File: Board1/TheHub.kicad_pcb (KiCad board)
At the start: 2 copper layers, 54 parts, among them J1 ARM_ADC_1, J10 SCIENCE + WHEELS POWER CONN, J11 RFD900, J12 I2C_1 Test Point, J13 I2C_2 Test Point, J14 ARDUINO NANO LEFT, J15 GPIO Test, J16 I2C_3 Test Point, J17 12V OUT, J18 7.4V IN, J19 ANALOG SENSORS, J2 ARM_ADC_2, J20 GPS, J21 COMPASS, J22 ARDUINO NANO RIGHT, J3 ARM_PWM_OUT, J4 ARM POWER CONN, J5 NucleoF411RE, J6 SCI_ADC_1, J7 SCIENCE_PWM_OUT, J8 12V MAIN POWER, J9 WHEEL_ADC_1, U1 PRE-PCA9685, U2 PRE-ADS1115, U3 PRE-ADS1115, U4 PRE-PCA9685, U5 PRE-ADS1115, U6 LD1086DT33TR, U7 LM340MP-5.0, U9 PRE-ADS1115

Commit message: Change 3v3 regulator, change appropriate pins to sockets
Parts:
- added J23: NucleoRight, Socket_Strips:Socket_Strip_Straight_2x19_Pitch2.54mm, F.Cu at (38.1, 43.2)
- J11: footprint Pin_Headers:Pin_Header_Angled_2x08_Pitch2.54mm -> Socket_Strips:Socket_Strip_Angled_2x08_Pitch2.54mm
- J14, J22: footprint Pin_Headers:Pin_Header_Straight_1x15_Pitch2.54mm -> Socket_Strips:Socket_Strip_Straight_1x15_Pitch2.54mm
- J20: footprint Pin_Headers:Pin_Header_Straight_1x09_Pitch2.54mm -> Socket_Strips:Socket_Strip_Straight_1x09_Pitch2.54mm
- J21: footprint Pin_Headers:Pin_Header_Straight_1x06_Pitch2.54mm -> Socket_Strips:Socket_Strip_Straight_1x06_Pitch2.54mm
- J5: value NucleoF411RE -> NucleoLeft; footprint Pin_Headers:Pin_Header_Straight_2x19_Pitch2.54mm -> Socket_Strips:Socket_Strip_Straight_2x19_Pitch2.54mm
- U2, U3, U5, U9: footprint Pin_Headers:Pin_Header_Straight_1x10_Pitch2.54mm -> Socket_Strips:Socket_Strip_Straight_1x10_Pitch2.54mm
- U6: value LD1086DT33TR -> TL1963; footprint TO_SOT_Packages_SMD:TO-252-3_TabPin2 -> TO_SOT_Packages_SMD:SOT-223-3Lead_TabPin2
- moved J21 252.2 mm to (0.00, 0.00)
- moved U6 117.3 mm to (0.00, 0.00)
- moved J5 62.6 mm to (22.9, 43.2)
- moved J11 18.3 mm to (74.9, 20.3), turned to 0 degrees
- moved J22 14.2 mm to (237.5, 34.3)
- moved J14 14.2 mm to (221.0, 34.3)
- moved J20 11.7 mm to (246.4, 49.5)
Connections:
- net /AGND renamed /PA4
- net /AVDD renamed /BOOT0
- net /PA10 renamed /VBAT
- net /PA2 renamed /PC2
- net /PA3 renamed /PC3
- net /PA5 renamed Net-(J5-Pad11)
- net /PB1 renamed Net-(J5-Pad24)
- net /PB13 renamed /PA1
- net /PB14 renamed /PA0
- net /PB15 renamed Net-(J5-Pad26)
- net /PB4 renamed /PC15
- net /PB5 renamed /PH0
- net /PB8 renamed /PC12
- net /PB9 renamed /VDD
- net /PC6 renamed /PD2
- net /PC8 renamed /PC11
- net Net-(J5-Pad36) renamed /PC1
- net Net-(J5-Pad38) renamed /PC0
- J5 pad 1: /PC9 -> /PC10
- J5 pad 12: /PA12 -> /IOREF
- J5 pad 13: /PA6 -> /PA13
- J5 pad 14: /PA11 -> /RESET
- J5 pad 15: /PA7 -> /PA14
- J5 pad 16: /PB12 -> +3V3
- J5 pad 17: /PB6 -> /PA15
- J5 pad 18: Net-(J5-Pad18) -> +5V
- J5 pad 21: /PA9 -> /PB7
- J5 pad 23: /PA8 -> /PC13
- J5 pad 25: /A5 -> /PC14
- J5 pad 31: /A4 -> /PH1
- J5 pad 34: /PC4 -> /PB0
- J5 pad 6: /PC5 -> /E5V
- J5 pad 9: GND -> Net-(J5-Pad9)
- U6 pad 1: GND -> +12V
- U6 pad 2: +3V3 -> GND
- U6 pad 3: +12V -> +3V3

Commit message: Create Layout placement forRFD900 and Nucleo
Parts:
- moved J23 355.4 mm to (389.9, 94.0)
- moved J11 318.9 mm to (393.7, 28.4)
- moved J5 310.3 mm to (328.9, 94.0)
- moved J21 248.0 mm to (246.4, 27.9)
- moved D7 7.18 mm to (214.6, 34.3)
- moved R13 5.08 mm to (214.6, 36.8)
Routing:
- net Net-(D7-Pad1): track 0.00 -> 3.39 mm
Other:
- board outline added: 195.6 x 195.6 mm
- board text added: "HEATSINK UP!"
- board text added: "RFD900"
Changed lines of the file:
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@@
   (general
     (links 255)
-    (no_connects 255)
+    (no_connects 254)
     (area 0 0 0 0)
     (thickness 1.6)
-    (drawings 0)
-    (tracks 0)
+    (drawings 21)
+    (tracks 3)
     (zones 0)
     (modules 55)
@@
   )
   (module LEDs:LED_0805 (layer F.Cu)
-    (at 209.55 39.37)
+    (at 214.63 34.29)
     (descr "LED 0805 smd package")
     (tags "LED led 0805 SMD smd SMT smt smdled SMDLED smtled SMTLED")
@@
   )
   (module Resistors_SMD:R_0805 (layer F.Cu)
-    (at 209.55 36.83)
+    (at 214.63 36.83)
     (descr "Resistor SMD 0805, reflow soldering, Vishay (see dcrcw.pdf)")
     (tags "resistor 0805")
@@
   )
   (module Socket_Strips:Socket_Strip_Straight_2x19_Pitch2.54mm (layer F.Cu)
-    (at 22.86 43.18)
+    (at 328.93 93.98)
     (descr "Through hole straight socket strip, 2x19, 2.54mm pitch, double rows")
     (tags "Through hole socket strip THT 2x19 2.54mm double row")
@@
   )
   (module Socket_Strips:Socket_Strip_Angled_2x08_Pitch2.54mm (layer F.Cu)
-    (at 74.93 20.32)
+    (at 393.7 28.448)
     (descr "Through hole angled socket strip, 2x08, 2.54mm pitch, 8.51mm socket length, double rows")
     (tags "Through hole angled socket strip THT 2x08 2.54mm double row")
@@
   )
   (module Socket_Strips:Socket_Strip_Straight_1x06_Pitch2.54mm (layer F.Cu)
-    (at 0 0)
+    (at 246.38 27.94)
     (descr "Through hole straight socket strip, 1x06, 2.54mm pitch, single row")
     (tags "Through hole socket strip THT 1x06 2.54mm single row")
@@
   )
   (module Socket_Strips:Socket_Strip_Straight_2x19_Pitch2.54mm (layer F.Cu)
-    (at 38.1 43.18)
+    (at 389.89 93.98)
     (descr "Through hole straight socket strip, 2x19, 2.54mm pitch, double rows")
     (tags "Through hole socket strip THT 2x19 2.54mm double row")
@@
     )
   )
+  (gr_line (start 323.85 59.69) (end 392.43 59.69) (angle 90) (layer F.SilkS) (width 0.2))
+  (gr_line (start 392.43 142.24) (end 323.85 142.24) (angle 90) (layer F.SilkS) (width 0.2))
+  (gr_line (start 392.43 142.24) (end 392.43 59.69) (angle 90) (layer F.SilkS) (width 0.2))
+  (gr_line (start 323.85 142.24) (end 323.85 59.69) (angle 90) (layer F.SilkS) (width 0.2))
+  (gr_text "HEATSINK UP!" (at 358.14 40.64) (layer F.SilkS)
+    (effects (font (size 1.5 1.5) (thickness 0.3)))
+  )
+  (gr_text RFD900 (at 358.14 35.56) (layer F.SilkS)
+    (effects (font (size 2.54 2.54) (thickness 0.508)))
+  )
+  (gr_line (start 322.58 44.45) (end 335.28 44.45) (angle 90) (layer F.SilkS) (width 0.2))
+  (gr_line (start 322.58 52.07) (end 322.58 44.45) (angle 90) (layer F.SilkS) (width 0.2))
+  (gr_line (start 335.28 52.07) (end 322.58 52.07) (angle 90) (layer F.SilkS) (width 0.2))
+  (gr_line (start 322.58 30.48) (end 335.28 30.48) (angle 90) (layer F.SilkS) (width 0.2))
+  (gr_line (start 322.58 22.86) (end 322.58 30.48) (angle 90) (layer F.SilkS) (width 0.2))
+  (gr_line (start 335.28 22.86) (end 322.58 22.86) (angle 90) (layer F.SilkS) (width 0.2))
+  (gr_line (start 335.28 21.59) (end 335.28 22.86) (angle 90) (layer F.SilkS) (width 0.2))
+  (gr_line (start 335.28 53.34) (end 381 53.34) (angle 90) (layer F.SilkS) (width 0.2))
+  (gr_line (start 335.28 21.59) (end 335.28 53.34) (angle 90) (layer F.SilkS) (width 0.2))
+  (gr_line (start 381 21.59) (end 335.28 21.59) (angle 90) (layer F.SilkS) (width 0.2))
+  (gr_line (start 381 53.34) (end 381 21.59) (angle 90) (layer F.SilkS) (width 0.2))
+  (gr_line (start 308.61 214.63) (end 308.61 19.05) (angle 90) (layer Edge.Cuts) (width 0.15))
+  (gr_line (start 504.19 214.63) (end 308.61 214.63) (angle 90) (layer Edge.Cuts) (width 0.15))
+  (gr_line (start 504.19 19.05) (end 504.19 214.63) (angle 90) (layer Edge.Cuts) (width 0.15))
+  (gr_line (start 308.61 19.05) (end 504.19 19.05) (angle 90) (layer Edge.Cuts) (width 0.15))
+  (segment (start 215.58 36.83) (end 215.58 36.51) (width 0.25) (layer F.Cu) (net 12))
+  (segment (start 215.58 36.51) (end 213.53 34.46) (width 0.25) (layer F.Cu) (net 12))
+  (segment (start 213.53 34.46) (end 213.53 34.29) (width 0.25) (layer F.Cu) (net 12))
 )

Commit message: Determine Main Board Layout
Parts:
- moved U6 422.2 mm to (416.6, 68.6)
- moved J8 408.5 mm to (497.8, 175.3), turned to 180 degrees
- moved R11 401.8 mm to (472.4, 110.5)
- moved R12 401.8 mm to (472.4, 106.7)
- moved J17 394.9 mm to (497.8, 182.9), turned to 180 degrees
- moved R10 387.4 mm to (450.9, 106.7)
- moved J18 384.6 mm to (497.8, 194.3), turned to 180 degrees
- moved R3 371.0 mm to (426.7, 110.5)
- moved R4 369.8 mm to (426.7, 106.7)
- moved R6 363.7 mm to (462.3, 82.5)
- moved R8 357.1 mm to (462.3, 90.2)
- moved R7 356.5 mm to (462.3, 86.4)
- moved J16 353.9 mm to (478.8, 110.5), turned to 180 degrees
- moved R5 351.8 mm to (450.9, 110.5)
- moved J13 322.6 mm to (457.2, 110.5), turned to 180 degrees
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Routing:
- net Net-(J3-Pad8): track 0.00 -> 10.8 mm
- net Net-(J3-Pad7): track 0.00 -> 10.8 mm
- net Net-(J3-Pad6): track 0.00 -> 10.8 mm
- net Net-(J3-Pad5): track 0.00 -> 10.8 mm
- net Net-(J3-Pad4): track 0.00 -> 9.72 mm
- net Net-(J3-Pad1): track 0.00 -> 9.72 mm
- net Net-(J3-Pad3): track 0.00 -> 9.72 mm
- net Net-(J3-Pad2): track 0.00 -> 9.72 mm

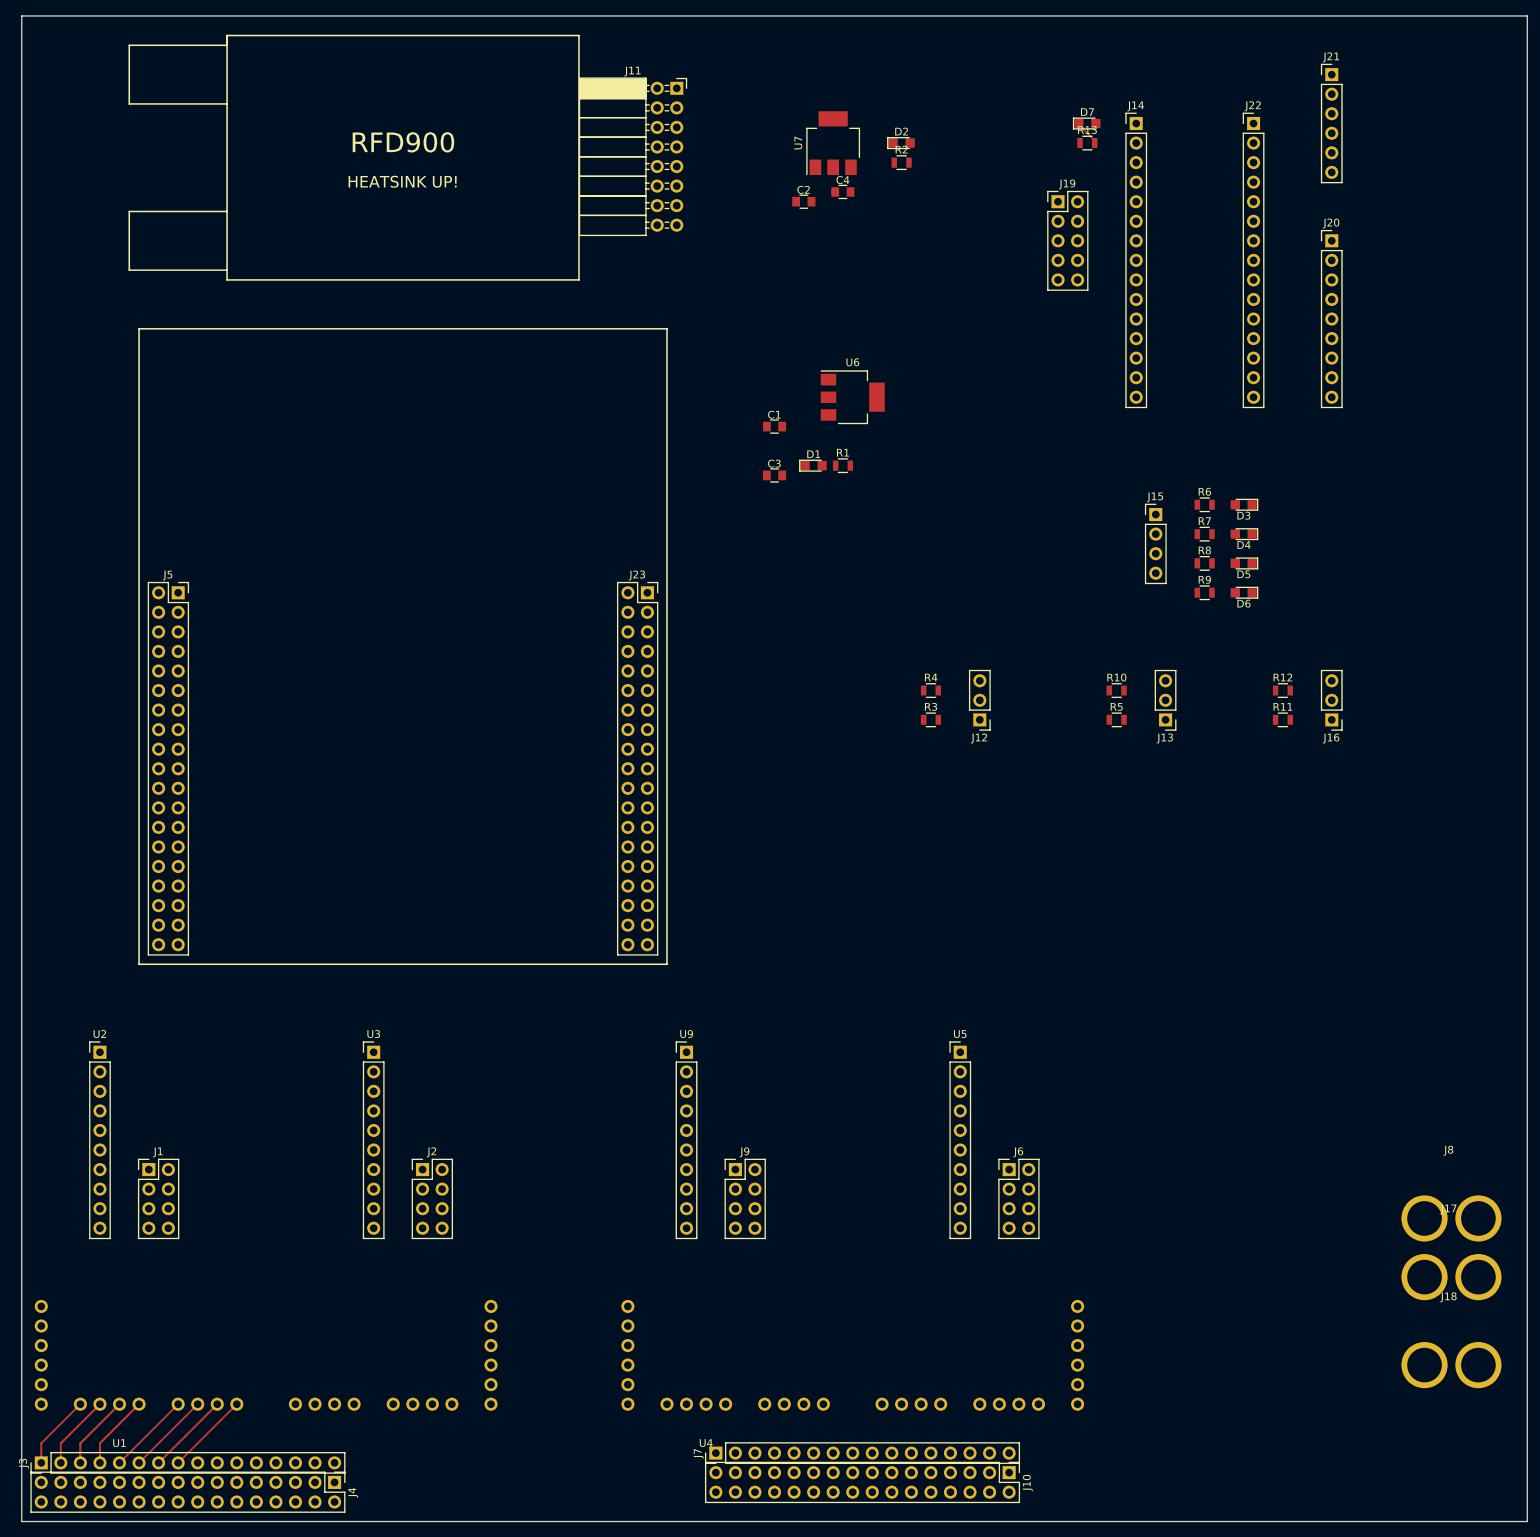
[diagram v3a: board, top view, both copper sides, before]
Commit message: Update nucleo headers to correct pin assignment
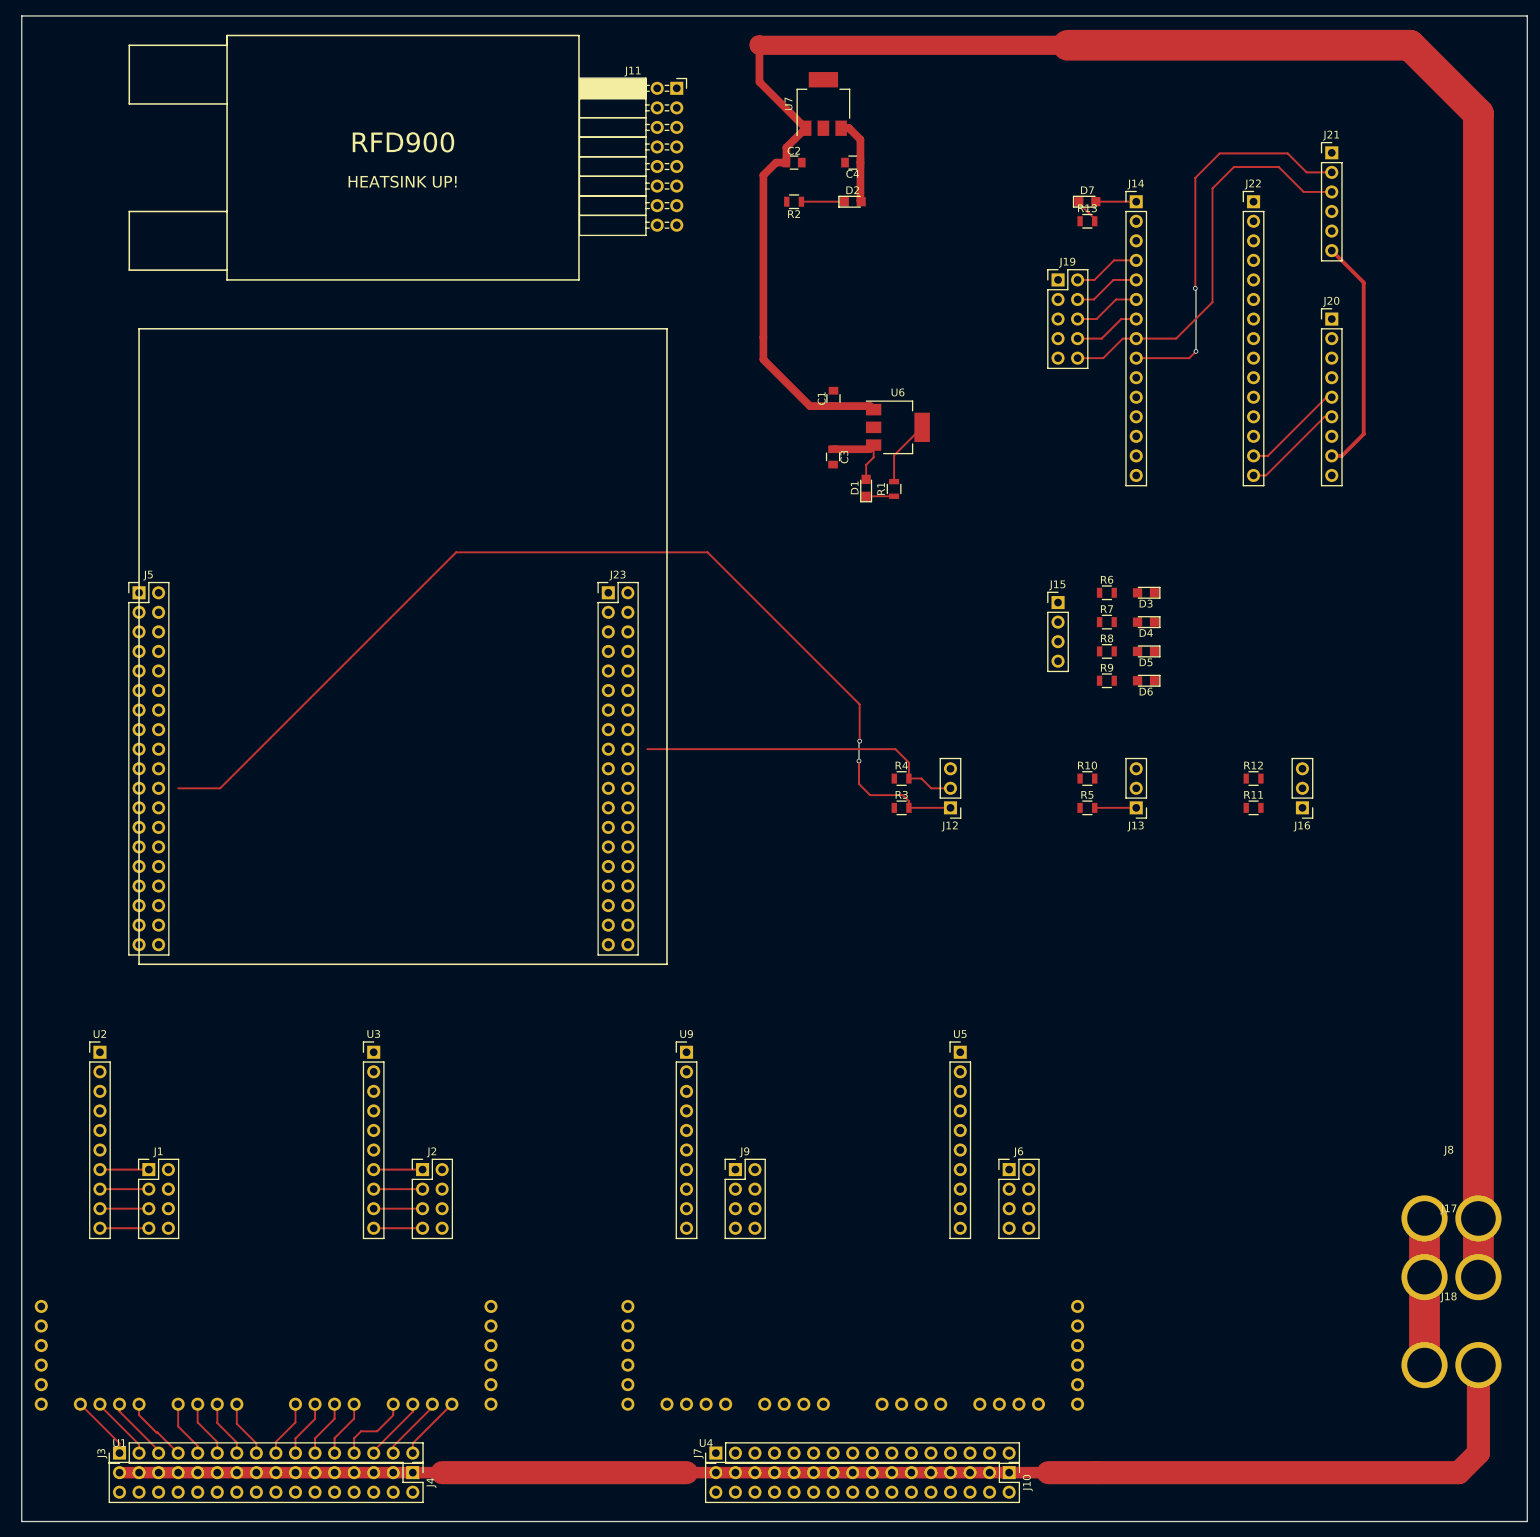
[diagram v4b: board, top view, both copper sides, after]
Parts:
- J23, J5: footprint Socket_Strips:Socket_Strip_Straight_2x19_Pitch2.54mm -> FoxWestern:NucleoSocketStrip
- moved D3 17.1 mm to (454.7, 94.0)
- moved D4 17.1 mm to (454.7, 97.8)
- moved J15 17.1 mm to (443.2, 95.2)
- moved R6 17.1 mm to (449.6, 94.0)
- moved R7 17.1 mm to (449.6, 97.8)
- moved D5 17.1 mm to (454.7, 101.6)
- moved D6 17.1 mm to (454.7, 105.4)
- moved R8 17.1 mm to (449.6, 101.6)
- moved R9 17.1 mm to (449.6, 105.4)
- moved R2 14.9 mm to (408.9, 43.2), turned to 180 degrees
- moved J12 12.0 mm to (429.3, 121.9)
- moved J13 12.0 mm to (453.4, 121.9)
- moved J16 12.0 mm to (475.0, 121.9)
- moved R11 12.0 mm to (468.6, 121.9)
- moved R3 12.0 mm to (422.9, 121.9)
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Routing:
- net +12V: track 0.00 -> 311.7 mm
- net /7.4V: track 0.00 -> 239.6 mm
- net /PB7: track 0.00 -> 133.5 mm, vias 0 -> 2
- net /A4: track 0.00 -> 58.7 mm
- net /A5: track 0.00 -> 50.8 mm, vias 0 -> 2
- net /PB6: track 0.00 -> 42.7 mm
- net +3V3: track 0.00 -> 41.2 mm
- net GND: track 0.00 -> 27.6 mm
- net /TX1: track 0.00 -> 13.3 mm
- net /RX0: track 0.00 -> 13.3 mm
- net +5V: track 0.00 -> 11.2 mm
- net Net-(J3-Pad13): track 0.00 -> 9.68 mm
- net /A0: track 0.00 -> 8.67 mm
- net /A3: track 0.00 -> 8.67 mm
- net /A2: track 0.00 -> 8.67 mm
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
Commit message: Finish Layout
RFD900 Is given insulated copper island to act as a heat spreader
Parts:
- moved C1 248.9 mm to (167.2, 100.0)
- moved D3 248.9 mm to (207.8, 125.2)
- moved D4 248.9 mm to (207.8, 129.0)
- moved D5 248.9 mm to (207.8, 132.8)
- moved D6 248.9 mm to (207.8, 136.7)
- moved D7 248.9 mm to (200.2, 74.4)
- moved J20 248.9 mm to (231.9, 89.7)
- moved J21 248.9 mm to (231.9, 68.1)
- moved J4 248.9 mm to (112.5, 239.5)
- moved R10 248.9 mm to (200.2, 149.4)
- moved R13 248.9 mm to (200.2, 77.0)
- moved R3 248.9 mm to (176.0, 153.2)
- moved R4 248.9 mm to (176.0, 149.4)
- moved R5 248.9 mm to (200.2, 153.2)
- moved U9 248.9 mm to (148.1, 184.9)
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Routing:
- net +3V3: track 41.2 -> 576.8 mm, vias 0 -> 9
- net /PB6: track 42.7 -> 354.4 mm, vias 0 -> 2
- net /PB7: track 133.5 -> 418.4 mm, vias 2 -> 3
- net /A5: track 50.8 -> 253.8 mm, vias 2 -> 5
- net /PA8: track 0.00 -> 171.0 mm, vias 0 -> 1
- net /A4: track 58.7 -> 227.3 mm, vias 0 -> 2
- net /PC9: track 0.00 -> 132.2 mm, vias 0 -> 2
- net /PC4: track 0.00 -> 92.3 mm, vias 0 -> 2
- net /PA11: track 0.00 -> 81.4 mm, vias 0 -> 1
- net /PA12: track 0.00 -> 74.8 mm, vias 0 -> 1
- net /PA7: track 0.00 -> 69.6 mm, vias 0 -> 1
- net /PA6: track 0.00 -> 69.1 mm, vias 0 -> 1
- net /PC5: track 0.00 -> 65.0 mm, vias 0 -> 1
- net GND: track 27.6 -> 45.9 mm, vias 0 -> 2
- net Net-(J7-Pad3): track 0.00 -> 10.5 mm
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- added copper zone on F.Cu, net (none)
- added copper zone on F.Cu, net +3V3
- added copper zone on F.Cu, net +5V
- added copper zone on B.Cu, net GND
